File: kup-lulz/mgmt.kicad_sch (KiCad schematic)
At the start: 25 parts, among them J14 PMOD_HOST, J37 XILINX_JTAG, J38 PMOD_HOST, J39 CONN_01X03, U14 STM32L431VxIx, U15 AT24MAC402, U9 XILINX_ULTRASCALEPLUS_B676

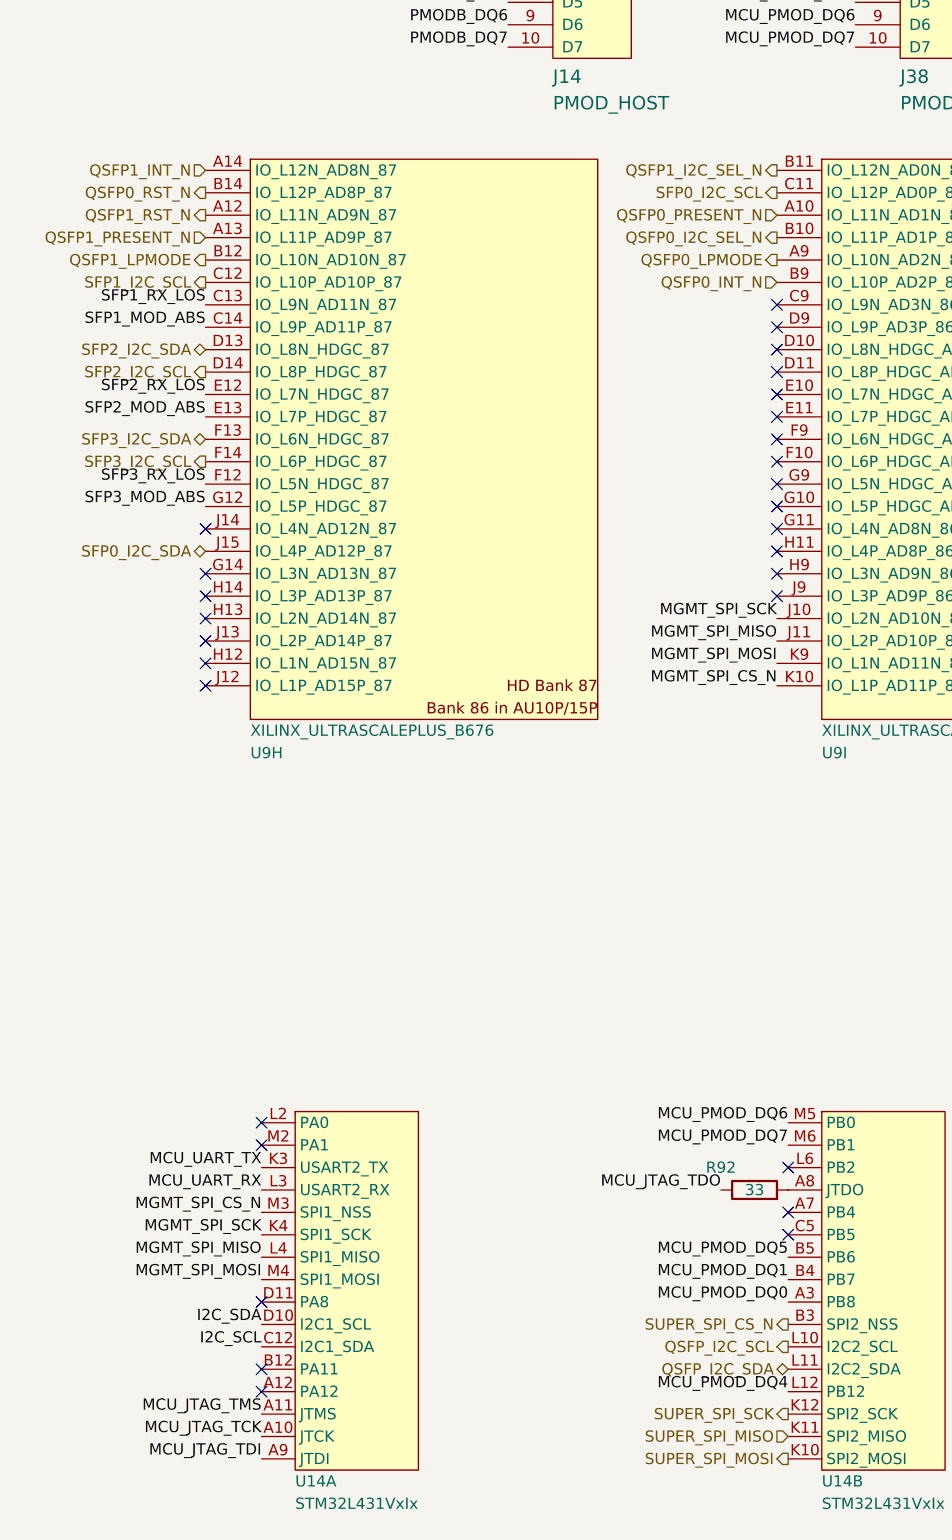
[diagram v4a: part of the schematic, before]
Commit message: Initial work on power planes, finished hooking up QSFP GPIOs
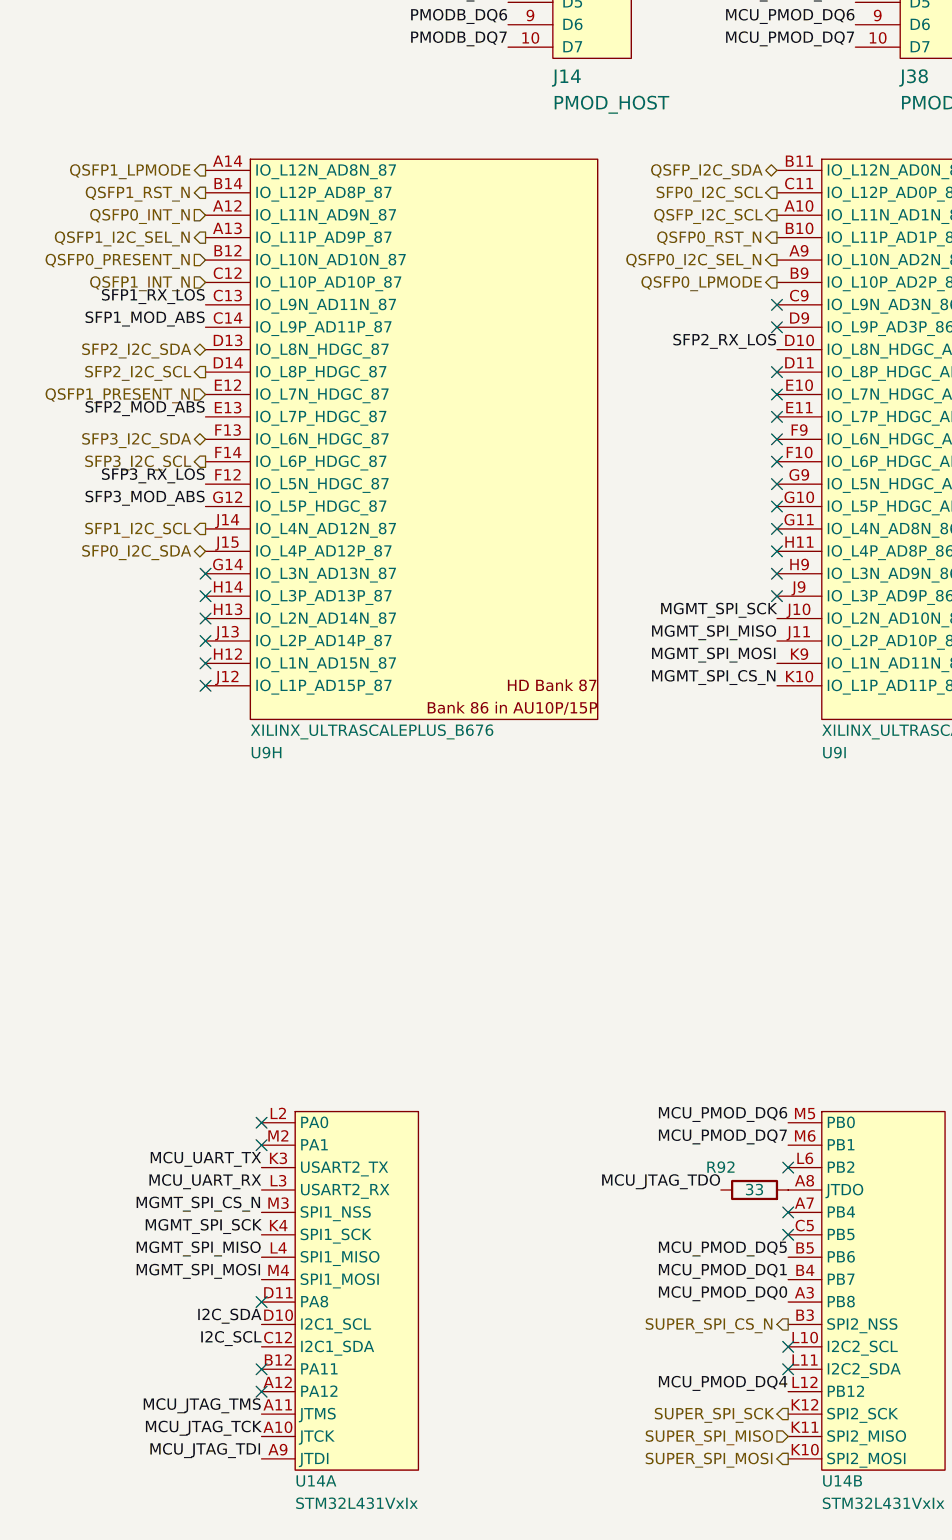
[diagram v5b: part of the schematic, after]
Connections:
- net QSFP0_I2C_SEL_N: now also U9.A9 (IO_L10N_AD2N_86); no longer U9.B10 (IO_L11P_AD1P_86)
- net QSFP0_INT_N: now also U9.A12 (IO_L11N_AD9N_87); no longer U9.B9 (IO_L10P_AD2P_86)
- net QSFP0_LPMODE: now also U9.B9 (IO_L10P_AD2P_86); no longer U9.A9 (IO_L10N_AD2N_86)
- net QSFP0_PRESENT_N: now also U9.B12 (IO_L10N_AD10N_87); no longer U9.A10 (IO_L11N_AD1N_86)
- net QSFP0_RST_N: now also U9.B10 (IO_L11P_AD1P_86); no longer U9.B14 (IO_L12P_AD8P_87)
- net QSFP1_I2C_SEL_N: now also U9.A13 (IO_L11P_AD9P_87); no longer U9.B11 (IO_L12N_AD0N_86)
- net QSFP1_INT_N: now also U9.C12 (IO_L10P_AD10P_87); no longer U9.A14 (IO_L12N_AD8N_87)
- net QSFP1_LPMODE: now also U9.A14 (IO_L12N_AD8N_87); no longer U9.B12 (IO_L10N_AD10N_87)
- net QSFP1_PRESENT_N: now also U9.E12 (IO_L7N_HDGC_87); no longer U9.A13 (IO_L11P_AD9P_87)
- net QSFP1_RST_N: now also U9.B14 (IO_L12P_AD8P_87); no longer U9.A12 (IO_L11N_AD9N_87)
- net QSFP_I2C_SCL: now also U9.A10 (IO_L11N_AD1N_86); no longer U14.L10 (PB10)
- net QSFP_I2C_SDA: now also U9.B11 (IO_L12N_AD0N_86); no longer U14.L11 (PB11)
- net SFP1_I2C_SCL: now also U9.J14 (IO_L4N_AD12N_87); no longer U9.C12 (IO_L10P_AD10P_87)
- net SFP2_RX_LOS: now also U9.D10 (IO_L8N_HDGC_AD4N_86); no longer U9.E12 (IO_L7N_HDGC_87)
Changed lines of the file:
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@@
   (no_connect (at 285.75 194.31))
   (no_connect (at 171.45 120.65))
-  (no_connect (at 101.6 82.55))
   (no_connect (at 36.83 118.11))
   (no_connect (at 101.6 92.71))
   (no_connect (at 101.6 97.79))
   (no_connect (at 153.67 179.07))
+  (no_connect (at 102.87 198.12))
   (no_connect (at 36.83 120.65))
   (no_connect (at 242.57 207.01))
@@
   (no_connect (at 101.6 107.95))
   (no_connect (at 171.45 105.41))
+  (no_connect (at 102.87 195.58))
   (no_connect (at 101.6 77.47))
   (no_connect (at 171.45 74.93))
@@
   (no_connect (at 171.45 62.23))
   (no_connect (at 43.18 170.18))
-  (no_connect (at 36.83 102.87))
   (no_connect (at 43.18 198.12))
   (wire (pts (xy 62.23 265.43) (xy 62.23 267.97))
@@
     (effects (font (size 1.27 1.27)) (justify left bottom))
   )
-  (label "SFP2_RX_LOS" (at 36.83 87.63 180)
+  (label "SFP2_RX_LOS" (at 101.6 82.55 180)
     (effects (font (size 1.27 1.27)) (justify right bottom))
   )
@@
     (effects (font (size 1.27 1.27)) (justify right bottom))
   )
-  (hierarchical_label "QSFP0_LPMODE" (shape output) (at 101.6 72.39 180)
+  (hierarchical_label "QSFP0_LPMODE" (shape output) (at 101.6 74.93 180)
     (effects (font (size 1.27 1.27)) (justify right))
   )
@@
     (effects (font (size 1.27 1.27)) (justify right))
   )
-  (hierarchical_label "QSFP0_RST_N" (shape output) (at 36.83 64.77 180)
+  (hierarchical_label "QSFP0_RST_N" (shape output) (at 101.6 69.85 180)
     (effects (font (size 1.27 1.27)) (justify right))
   )
@@
     (effects (font (size 1.27 1.27)) (justify right))
   )
-  (hierarchical_label "QSFP1_INT_N" (shape input) (at 36.83 62.23 180)
+  (hierarchical_label "QSFP1_INT_N" (shape input) (at 36.83 74.93 180)
     (effects (font (size 1.27 1.27)) (justify right))
   )
@@
     (effects (font (size 1.27 1.27)) (justify right))
   )
-  (hierarchical_label "QSFP_I2C_SDA" (shape bidirectional) (at 102.87 198.12 180)
+  (hierarchical_label "QSFP_I2C_SDA" (shape bidirectional) (at 101.6 62.23 180)
     (effects (font (size 1.27 1.27)) (justify right))
   )
@@
     (effects (font (size 1.27 1.27)) (justify right))
   )
-  (hierarchical_label "QSFP1_RST_N" (shape output) (at 36.83 67.31 180)
-    (effects (font (size 1.27 1.27)) (justify right))
-  )
-  (hierarchical_label "QSFP1_PRESENT_N" (shape input) (at 36.83 69.85 180)
+  (hierarchical_label "QSFP1_RST_N" (shape output) (at 36.83 64.77 180)
+    (effects (font (size 1.27 1.27)) (justify right))
+  )
+  (hierarchical_label "QSFP1_PRESENT_N" (shape input) (at 36.83 87.63 180)
     (effects (font (size 1.27 1.27)) (justify right))
   )
@@
     (effects (font (size 1.27 1.27)) (justify right))
   )
-  (hierarchical_label "QSFP1_I2C_SEL_N" (shape output) (at 101.6 62.23 180)
+  (hierarchical_label "QSFP1_I2C_SEL_N" (shape output) (at 36.83 69.85 180)
     (effects (font (size 1.27 1.27)) (justify right))
   )
@@
     (effects (font (size 1.27 1.27)) (justify right))
   )
-  (hierarchical_label "QSFP_I2C_SCL" (shape output) (at 102.87 195.58 180)
+  (hierarchical_label "QSFP_I2C_SCL" (shape output) (at 101.6 67.31 180)
     (effects (font (size 1.27 1.27)) (justify right))
   )
@@
     (effects (font (size 1.27 1.27)) (justify right))
   )
-  (hierarchical_label "QSFP1_LPMODE" (shape output) (at 36.83 72.39 180)
+  (hierarchical_label "QSFP1_LPMODE" (shape output) (at 36.83 62.23 180)
     (effects (font (size 1.27 1.27)) (justify right))
   )
@@
     (effects (font (size 1.27 1.27)) (justify right))
   )
-  (hierarchical_label "QSFP0_INT_N" (shape input) (at 101.6 74.93 180)
+  (hierarchical_label "QSFP0_INT_N" (shape input) (at 36.83 67.31 180)
     (effects (font (size 1.27 1.27)) (justify right))
   )
@@
     (effects (font (size 1.27 1.27)) (justify right))
   )
-  (hierarchical_label "QSFP0_PRESENT_N" (shape input) (at 101.6 67.31 180)
+  (hierarchical_label "QSFP0_PRESENT_N" (shape input) (at 36.83 72.39 180)
     (effects (font (size 1.27 1.27)) (justify right))
   )
@@
     (effects (font (size 1.27 1.27)) (justify right))
   )
-  (hierarchical_label "QSFP0_I2C_SEL_N" (shape output) (at 101.6 69.85 180)
+  (hierarchical_label "QSFP0_I2C_SEL_N" (shape output) (at 101.6 72.39 180)
     (effects (font (size 1.27 1.27)) (justify right))
   )
@@
     (effects (font (size 1.27 1.27)) (justify right))
   )
-  (hierarchical_label "SFP1_I2C_SCL" (shape output) (at 36.83 74.93 180)
-    (effects (font (size 1.27 1.27)) (justify right))
-  )
+  (hierarchical_label "SFP1_I2C_SCL" (shape output) (at 36.83 102.87 180)
+    (effects (font (size 1.27 1.27)) (justify right))
+  )
